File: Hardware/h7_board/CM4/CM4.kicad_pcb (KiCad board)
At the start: 4 copper layers, 68.2 x 41.6 mm, 85 parts, among them IC1 OPA659IDBVR, IC2 OPA659IDBVR, IC3 LMH6643MAX_NOPB, IC4 TPS65133DPDR, IC5 TPS62111RSAT, J1 Conn_Coaxial, J2 USB_C_Receptacle_USB2.0, J3 SWDIO, J4 Micro_SD_Card, J5 PREAMP, J6 BIASED OUTPUT, J7 USART, Q1 AO3401A, U1 USBLC6-2SC6, U2 STM32H743VITx, U3 REF3433IDBVR, Y1 16MHz

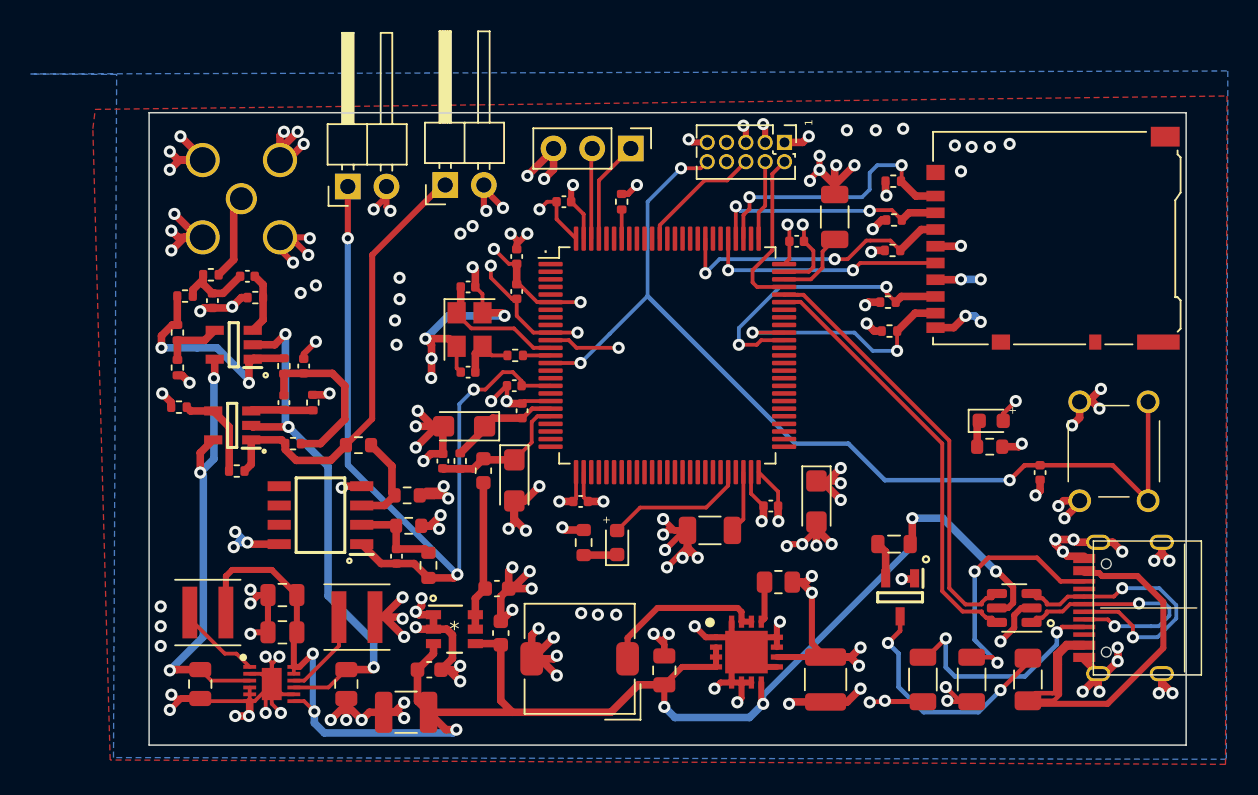
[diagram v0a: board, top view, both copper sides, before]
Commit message: Edited Design to modify to LDO regulator and improve board layout
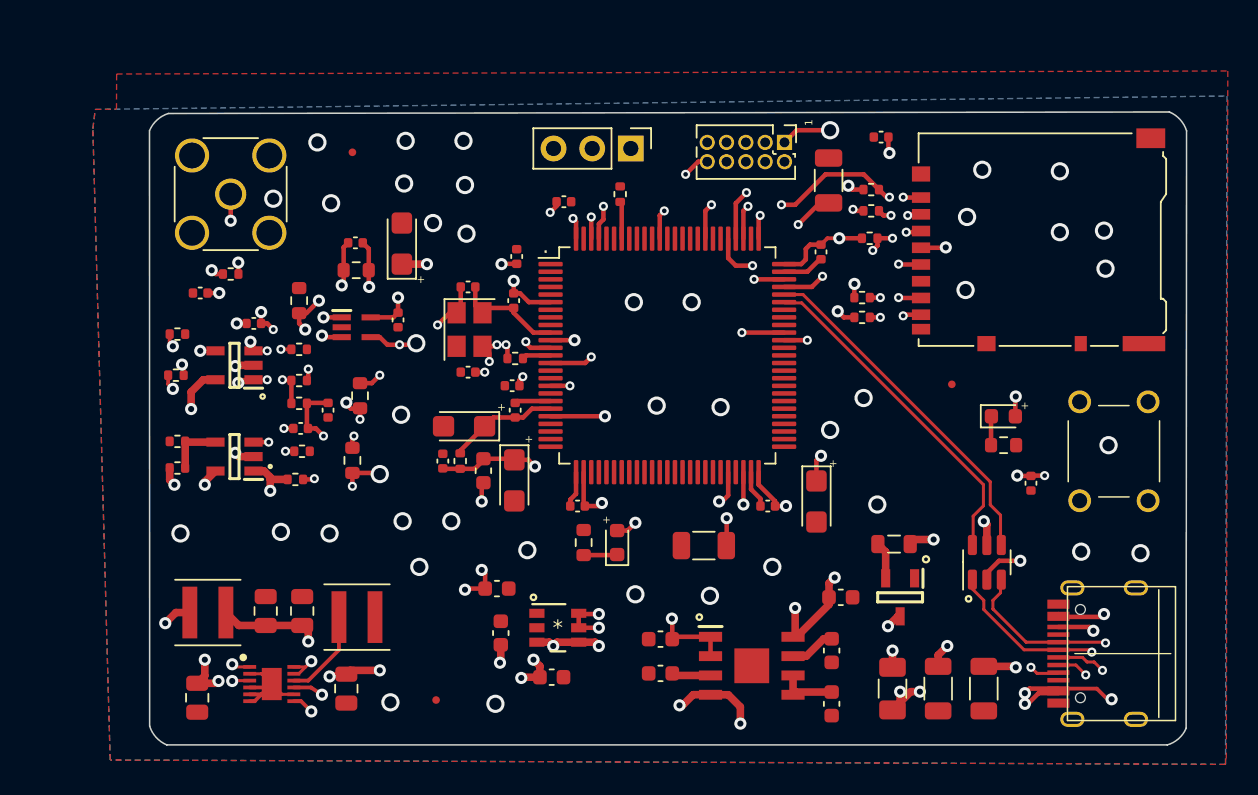
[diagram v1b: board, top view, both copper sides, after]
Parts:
- removed J5: PREAMP, Connector_PinHeader_2.54mm:PinHeader_1x02_P2.54mm_Horizontal
- removed J6: BIASED OUTPUT, Connector_PinHeader_2.54mm:PinHeader_1x02_P2.54mm_Horizontal
- removed L3: 6.8u, Inductor_SMD:L_TDK_SLF7032
- removed R25, R26: 47k, Resistor_SMD:R_0402_1005Metric
- removed U1: USBLC6-2SC6, Package_TO_SOT_SMD:SOT-23-6
- added C30: 100p, Capacitor_SMD:C_0402_1005Metric, F.Cu at (99.5, 87.0)
- added C31: 100p, Capacitor_SMD:C_0402_1005Metric, F.Cu at (109.7, 83.7)
- added C32: 10u, Capacitor_Tantalum_SMD:CP_EIA-3216-18_Kemet-A, F.Cu at (112.8, 83.8)
- added C33: 100n, Capacitor_SMD:C_0402_1005Metric, F.Cu at (112.5, 88.8)
- added C34: 100n, Capacitor_SMD:C_0402_1005Metric, F.Cu at (144.2, 76.8)
- added FID1: Fiducial, Fiducial:Fiducial_0.5mm_Mask1.5mm, F.Cu at (109.5, 77.8)
- added FID2: Fiducial, Fiducial:Fiducial_0.5mm_Mask1.5mm, F.Cu at (115.0, 113.8)
- added FID3: Fiducial, Fiducial:Fiducial_0.5mm_Mask1.5mm, F.Cu at (148.9, 93.0)
- added R19: 47k, Resistor_SMD:R_0402_1005Metric, F.Cu at (143.6, 81.6)
- added U4: USBLC6-2SC6, Package_TO_SOT_SMD:SOT-23-6, F.Cu at (151.2, 104.7)
- C1, C2: value 100p -> 10u; footprint Capacitor_SMD:C_0402_1005Metric -> Capacitor_SMD:C_0603_1608Metric
- C10: value 10u x5R 25V -> 100p; footprint Capacitor_SMD:C_1210_3225Metric -> Capacitor_SMD:C_0402_1005Metric
- C11: value 22u x7R 10V -> 100p; footprint Capacitor_SMD:C_1210_3225Metric -> Capacitor_SMD:C_0402_1005Metric
- C12: value 1u -> 100p; footprint Capacitor_SMD:C_0805_2012Metric -> Capacitor_SMD:C_0402_1005Metric
- C3, C4: value 100p -> 1u; footprint Capacitor_SMD:C_0402_1005Metric -> Capacitor_SMD:C_0603_1608Metric
- C5: value 10p -> 1u; footprint Capacitor_SMD:C_0402_1005Metric -> Capacitor_SMD:C_0603_1608Metric
- IC1: value OPA659IDBVR -> ADP7156ARDZ-3.3-R7; footprint SamacSys_Parts:SOT95P280X145-5N -> SamacSys_Parts:SOIC127P600X175-9N
- IC3: value LMH6643MAX_NOPB -> OPA659IDBVR; footprint SamacSys_Parts:SOIC127P600X175-8N -> SamacSys_Parts:SOT95P280X145-5N
- IC5: value TPS62111RSAT -> OPA377AIDCKR; footprint SamacSys_Parts:QFN65P400X400X100-17N-D -> SamacSys_Parts:SOT65P210X110-5N
- J1: value Conn_Coaxial -> USB_C_Receptacle_USB2.0; footprint Connector_Coaxial:SMA_Wurth_60312002114503_Vertical -> CM4IO:TYPE-C-31-M-12; moved to F.Cu
- J2: value USB_C_Receptacle_USB2.0 -> Conn_Coaxial; footprint CM4IO:TYPE-C-31-M-12 -> Connector_Coaxial:SMA_Wurth_60312002114503_Vertical
- R1: value 44.2k -> 5.1k; footprint Resistor_SMD:R_0402_1005Metric -> Resistor_SMD:R_1206_3216Metric
- R11: value 100k -> 187; footprint Resistor_SMD:R_0603_1608Metric -> Resistor_SMD:R_0402_1005Metric
- R12: value 50k -> 2.49k; footprint Resistor_SMD:R_0603_1608Metric -> Resistor_SMD:R_0402_1005Metric
- R15: value 5.1k -> 49.9k; footprint Resistor_SMD:R_1206_3216Metric -> Resistor_SMD:R_0603_1608Metric
- R16: value 5.1k -> 100k; footprint Resistor_SMD:R_1206_3216Metric -> Resistor_SMD:R_0603_1608Metric
- R17: value 1M -> 47k; footprint Resistor_SMD:R_0805_2012Metric -> Resistor_SMD:R_0402_1005Metric
- R2: value 66.5k -> 5.1k; footprint Resistor_SMD:R_0402_1005Metric -> Resistor_SMD:R_1206_3216Metric
- R3: value 6.34k -> 44.2k
- R4: value 35.7k -> 66.5k
- R5: value 34.8k -> 6.34k
- R6: value 10k -> 35.7k
- R7: value 187 -> 34.8k
- R8: value 2.49k -> 10k
- U3: footprint footprints:REF3433IDBVR -> REF3433:REF3433IDBVR
- moved J2 67.0 mm to (101.5, 80.5), turned to 0 degrees
- moved J1 66.0 mm to (161.0, 110.7)
- moved R2 55.8 mm to (148.0, 113.0), turned to -90 degrees
- moved R16 50.7 mm to (106.0, 87.5), turned to 90 degrees
- moved R1 48.2 mm to (151.0, 113.0), turned to -90 degrees
- moved R15 45.9 mm to (109.8, 85.5), turned to 180 degrees
- moved C2 44.3 mm to (141.6, 107.0), turned to 0 degrees
- moved C11 44.3 mm to (103.0, 89.0), turned to 0 degrees
- moved C3 39.4 mm to (141.0, 110.5), turned to -90 degrees
- moved C4 38.3 mm to (129.8, 112.0), turned to 180 degrees
- moved IC1 37.6 mm to (135.8, 111.5), turned to 0 degrees
- moved IC5 33.4 mm to (109.8, 89.2)
- moved C5 30.2 mm to (141.0, 114.0)
- moved C1 29.2 mm to (129.8, 109.8), turned to 180 degrees
- moved C12 27.9 mm to (107.9, 94.7), turned to -90 degrees
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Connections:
- C1 pad 1: Net-(C1-Pad1) -> /+3.3V
- C1 pad 2: Net-(C1-Pad2) -> GND
- C10 pad 1: /Power/+5V -> Net-(C10-Pad1)
- C10 pad 2: GND -> Net-(C10-Pad2)
- C11 pad 1: /+3.3V -> Net-(C11-Pad1)
- C11 pad 2: GND -> Net-(C11-Pad2)
- C12 pad 1: /Power/+5V -> Net-(C10-Pad2)
- C2 pad 1: Net-(C2-Pad1) -> /Power/+5V
- C2 pad 2: Net-(C2-Pad2) -> GND
- C3 pad 1: Net-(C1-Pad2) -> Net-(C3-Pad1)
- C4 pad 1: Net-(C2-Pad2) -> Net-(C4-Pad1)
- C5 pad 2: /v_DIV_OUT -> GND
- IC1 pad 1: P_AMP_OUT -> /+3.3V
- IC1 pad 2: /VNEG -> /+3.3V
- IC1 pad 3: Net-(C1-Pad1) -> Net-(C4-Pad1)
- IC1 pad 4: Net-(IC1-Pad4) -> /Power/+5V
- IC1 pad 5: /VPOS -> Net-(C5-Pad1)
- IC2 pad 1: Net-(IC2-Pad1) -> P_AMP_OUT
- IC2 pad 3: Net-(C2-Pad1) -> Net-(C10-Pad1)
- IC3 pad 1: /v_DIV_OUT -> Net-(IC3-Pad1)
- IC3 pad 2: Net-(C5-Pad1) -> /VNEG
- IC3 pad 3: Net-(IC3-Pad3) -> Net-(C11-Pad1)
- IC3 pad 4: GND -> Net-(IC3-Pad4)
- IC3 pad 5: no_connect_55 -> /VPOS
- IC5 pad 1: GND -> Net-(IC5-Pad1)
- IC5 pad 2: /Power/+5V -> GND
- IC5 pad 3: /Power/+5V -> Net-(C31-Pad2)
- IC5 pad 4: /Power/+5V -> /v_DIV_OUT
- IC5 pad 5: GND -> /+3.3V
- J3 pad 7: no_connect_60 -> no_connect_58
- J3 pad 8: no_connect_61 -> no_connect_59
- R1 pad 1: P_AMP_OUT -> Net-(J1-PadA5)
- R1 pad 2: Net-(C1-Pad2) -> GND
- R10 pad 1: Net-(IC2-Pad1) -> P_AMP_OUT
- R11 pad 1: GND -> Net-(IC3-Pad4)
- R11 pad 2: Net-(C5-Pad1) -> GND
- R12 pad 1: /v_DIV_OUT -> Net-(IC3-Pad1)
- R12 pad 2: Net-(C5-Pad1) -> Net-(IC3-Pad4)
- R13 pad 1: Net-(IC3-Pad3) -> Net-(IC5-Pad1)
- R14 pad 2: Net-(IC3-Pad3) -> Net-(IC5-Pad1)
- R15 pad 1: Net-(J2-PadA5) -> /v_DIV_OUT
- R15 pad 2: GND -> Net-(C31-Pad2)
- R16 pad 1: Net-(J2-PadB5) -> Net-(C31-Pad2)
- R17 pad 1: /Power/PG -> /H7MCU/SDMMC_D2
- R2 pad 1: Net-(IC2-Pad1) -> Net-(J1-PadB5)
- R2 pad 2: Net-(C2-Pad2) -> GND
- R22 pad 1: /H7MCU/SDMMC_D2 -> /H7MCU/SDMMC_CMD
- R23 pad 1: /H7MCU/SDMMC_D3 -> /H7MCU/SDMMC_D0
- R24 pad 1: /H7MCU/SDMMC_CMD -> /H7MCU/SDMMC_D1
- R3 pad 1: GND -> P_AMP_OUT
- R3 pad 2: Net-(C1-Pad1) -> Net-(C10-Pad2)
- R4 pad 1: Net-(C2-Pad2) -> Net-(IC3-Pad1)
- R4 pad 2: Net-(J1-Pad1) -> Net-(C11-Pad2)
- R5 pad 1: Net-(C1-Pad2) -> GND
- R5 pad 2: Net-(IC2-Pad1) -> Net-(C10-Pad1)
- R6 pad 1: GND -> Net-(C11-Pad2)
- R6 pad 2: Net-(C2-Pad1) -> Net-(J2-Pad1)
- R7 pad 1: Net-(IC1-Pad4) -> Net-(C10-Pad2)
- R7 pad 2: GND -> Net-(IC3-Pad1)
- R8 pad 1: P_AMP_OUT -> GND
- R8 pad 2: Net-(IC1-Pad4) -> Net-(C11-Pad1)
- U2 pad 1: no_connect_62 -> no_connect_60
- U2 pad 15: no_connect_63 -> no_connect_61
- U2 pad 16: no_connect_64 -> no_connect_62
- U2 pad 18: no_connect_65 -> no_connect_63
- U2 pad 2: no_connect_66 -> no_connect_64
- U2 pad 22: no_connect_67 -> no_connect_65
- U2 pad 23: no_connect_68 -> no_connect_66
- U2 pad 24: no_connect_69 -> no_connect_67
- U2 pad 25: no_connect_70 -> no_connect_68
- U2 pad 28: no_connect_71 -> no_connect_69
- U2 pad 29: no_connect_72 -> no_connect_70
- U2 pad 3: no_connect_73 -> no_connect_71
- U2 pad 30: no_connect_74 -> no_connect_72
- U2 pad 31: no_connect_75 -> no_connect_73
- U2 pad 32: no_connect_76 -> no_connect_74
- U2 pad 33: no_connect_77 -> no_connect_75
- U2 pad 34: no_connect_78 -> no_connect_76
- U2 pad 35: no_connect_79 -> no_connect_77
- U2 pad 36: no_connect_80 -> no_connect_78
- U2 pad 37: no_connect_81 -> no_connect_79
- U2 pad 38: no_connect_82 -> no_connect_80
- U2 pad 39: no_connect_83 -> no_connect_81
- U2 pad 4: no_connect_84 -> no_connect_82
- U2 pad 40: no_connect_85 -> no_connect_83
- U2 pad 41: no_connect_86 -> no_connect_84
- U2 pad 42: no_connect_87 -> no_connect_85
- U2 pad 43: no_connect_88 -> no_connect_86
- U2 pad 44: no_connect_89 -> no_connect_87
- U2 pad 45: no_connect_90 -> no_connect_88
- U2 pad 47: no_connect_91 -> no_connect_89
- U2 pad 5: no_connect_92 -> no_connect_90
- U2 pad 51: no_connect_93 -> no_connect_91
- U2 pad 52: no_connect_94 -> no_connect_92
- U2 pad 53: no_connect_95 -> no_connect_93
- U2 pad 54: no_connect_96 -> no_connect_94
- U2 pad 55: no_connect_97 -> no_connect_95
- U2 pad 56: no_connect_98 -> no_connect_96
- U2 pad 57: no_connect_99 -> no_connect_97
- U2 pad 58: no_connect_100 -> no_connect_98
- U2 pad 59: no_connect_101 -> no_connect_99
- U2 pad 60: no_connect_102 -> no_connect_100
- U2 pad 61: no_connect_103 -> no_connect_101
- U2 pad 62: no_connect_104 -> no_connect_102
- U2 pad 63: no_connect_105 -> no_connect_103
- U2 pad 64: no_connect_106 -> no_connect_104
- U2 pad 67: no_connect_107 -> no_connect_105
- U2 pad 68: no_connect_108 -> no_connect_106
- U2 pad 69: no_connect_109 -> no_connect_107
- U2 pad 7: no_connect_110 -> no_connect_108
- U2 pad 77: no_connect_111 -> no_connect_109
- U2 pad 8: no_connect_112 -> no_connect_110
- U2 pad 81: no_connect_113 -> no_connect_111
- U2 pad 82: no_connect_114 -> no_connect_112
- U2 pad 84: no_connect_115 -> no_connect_113
- U2 pad 85: no_connect_116 -> no_connect_114
- U2 pad 86: no_connect_117 -> no_connect_115
- U2 pad 87: no_connect_118 -> no_connect_116
- U2 pad 88: no_connect_119 -> no_connect_117
- U2 pad 9: no_connect_120 -> no_connect_118
- U2 pad 90: no_connect_121 -> no_connect_119
- U2 pad 91: no_connect_122 -> no_connect_120
- U2 pad 92: no_connect_123 -> no_connect_121
- U2 pad 93: no_connect_124 -> no_connect_122
- U2 pad 95: no_connect_125 -> no_connect_123
- U2 pad 96: no_connect_126 -> no_connect_124
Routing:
- net GND: track 295.8 -> 26.6 mm, vias 156 -> 40
- net /+3.3V: track 75.2 -> 47.1 mm, vias 31 -> 21
- net /v_DIV_OUT: track 54.5 -> 27.1 mm, vias 3 -> 5
- net /Power/+5V: track 105.4 -> 86.6 mm, vias 7 -> 14
- net Net-(J2-PadB5): track 16.7 -> 0.00 mm, vias 2 -> 0
- net Net-(J2-PadA5): track 15.1 -> 0.00 mm, vias 2 -> 0
- net Net-(IC2-Pad1): track 14.6 -> 0.00 mm, vias 2 -> 0
- net Net-(J1-PadB5): track 0.00 -> 14.0 mm, vias 0 -> 2
- net Net-(C11-Pad2): track 0.00 -> 12.7 mm, vias 0 -> 5
- net /3.3VREF: track 9.94 -> 22.2 mm, vias 0 -> 5
- net Net-(F1-Pad2): track 16.1 -> 3.89 mm
- net Net-(IC5-Pad1): track 0.00 -> 11.8 mm, vias 0 -> 4
- net Net-(C1-Pad2): track 11.5 -> 0.00 mm
- net Net-(IC3-Pad1): track 0.00 -> 11.4 mm, vias 0 -> 4
- net /Power/SW: track 11.1 -> 0.00 mm
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- added copper zone on In1.Cu, net /+3.3V
- removed copper zone on In1.Cu, net GND
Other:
- outline, holes or cut-outs redrawn
- board text removed: "BIASED SIGNAL"

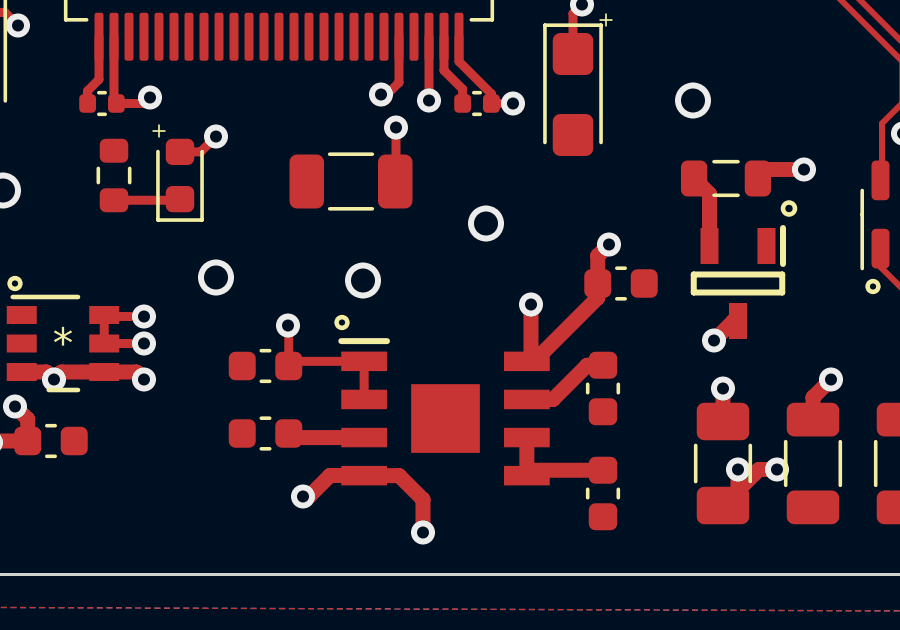
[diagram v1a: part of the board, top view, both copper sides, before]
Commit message: Added Low noise analysis and design files
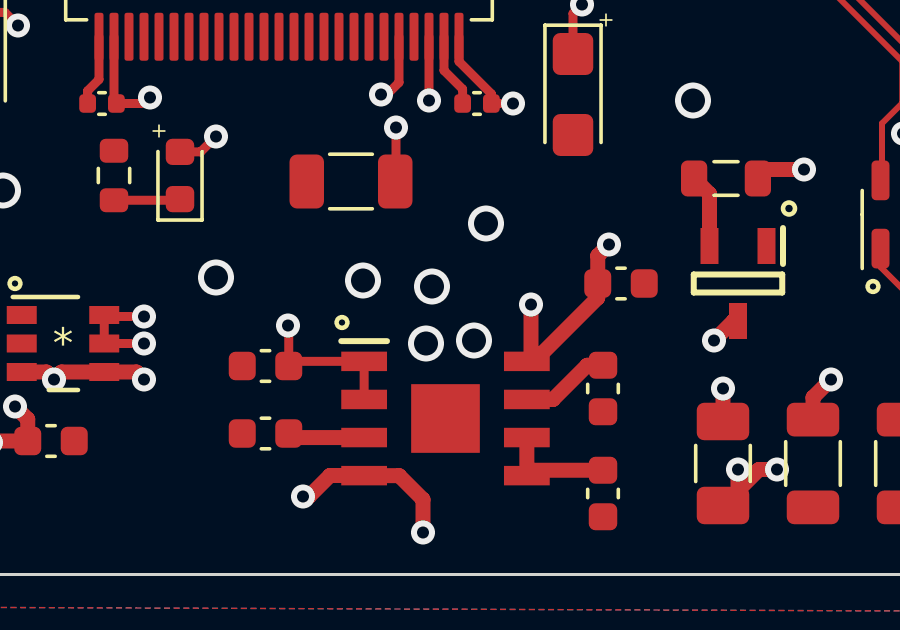
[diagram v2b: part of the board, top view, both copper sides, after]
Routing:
- net GND: vias 40 -> 43
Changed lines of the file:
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@@
     (descr "Tantalum Capacitor SMD Kemet-A (3216-18 Metric), IPC_7351 nominal, (Body size from: http://www.kemet.com/Lists/ProductCatalog/Attachments/253/KEM_TC101_STD.pdf), generated with kicad-footprint-generator")
     (tags "capacitor tantalum")
+    (property "LCSC Part #" "C7171")
     (property "Sheet file" "preamp.kicad_sch")
     (property "Sheet name" "Preamp")
@@
     (at 161 110.7 90)
     (descr "Korean Hroparts Elec, Power only USB connector supporting up to 3A")
+    (property "LCSC Part #" " C165948")
     (property "Sheet file" "power.kicad_sch")
     (property "Sheet name" "Power")
@@
     (descr "Capacitor SMD 0603 (1608 Metric), square (rectangular) end terminal, IPC_7351 nominal, (Body size source: IPC-SM-782 page 76, https://www.pcb-3d.com/wordpress/wp-content/uploads/ipc-sm-782a_amendment_1_and_2.pdf), generated with kicad-footprint-generator")
     (tags "capacitor")
-    (property "LCSC Part #" "C15849")
+    (property "LCSC Part #" "C19702")
     (property "Sheet file" "power.kicad_sch")
     (property "Sheet name" "Power")
@@
     (descr "Capacitor SMD 0603 (1608 Metric), square (rectangular) end terminal, IPC_7351 nominal, (Body size source: IPC-SM-782 page 76, https://www.pcb-3d.com/wordpress/wp-content/uploads/ipc-sm-782a_amendment_1_and_2.pdf), generated with kicad-footprint-generator")
     (tags "capacitor")
-    (property "LCSC Part #" "C15849")
+    (property "LCSC Part #" "C19702")
     (property "Sheet file" "power.kicad_sch")
     (property "Sheet name" "Power")
@@
   (via (at 108.1 81.1) (size 1.2) (drill 0.8) (layers "F.Cu" "B.Cu") (free) (net 1))
   (via (at 121 103.9) (size 1.2) (drill 0.8) (layers "F.Cu" "B.Cu") (free) (net 1))
+  (via (at 135.1 109) (size 1.2) (drill 0.8) (layers "F.Cu" "B.Cu") (free) (net 1))
+  (via (at 135.3 107.1) (size 1.2) (drill 0.8) (layers "F.Cu" "B.Cu") (free) (net 1))
   (via (at 159.2 97) (size 1.2) (drill 0.8) (layers "F.Cu" "B.Cu") (free) (net 1))
   (via (at 114.8 82.4) (size 1.2) (drill 0.8) (layers "F.Cu" "B.Cu") (free) (net 1))
@@
   (via (at 104.3 80.8) (size 1.2) (drill 0.8) (layers "F.Cu" "B.Cu") (free) (net 1))
   (via (at 143.1 93.9) (size 1.2) (drill 0.8) (layers "F.Cu" "B.Cu") (free) (net 1))
+  (via (at 136.7 108.9) (size 1.2) (drill 0.8) (layers "F.Cu" "B.Cu") (free) (net 1))
   (via (at 118.9 114) (size 1.2) (drill 0.8) (layers "F.Cu" "B.Cu") (free) (net 1))
   (via (at 158.9 82.9) (size 1.2) (drill 0.8) (layers "F.Cu" "B.Cu") (free) (net 1))
@@
   (segment (start 136.6 81.6) (end 136.6 78.4) (width 0.3) (layer "In1.Cu") (net 70))
   (segment (start 136.3 81.9) (end 136.6 81.6) (width 0.3) (layer "In1.Cu") (net 70))
-  (segment (start 136.6 78.4) (end 136.63 78.37) (width 0.3) (layer "In1.Cu") (net 70))
   (segment (start 139.7 86.6) (end 140.4 85.9) (width 0.3) (layer "F.Cu") (net 71))
   (segment (start 137.875 86.6) (end 139.7 86.6) (width 0.3) (layer "F.Cu") (net 71))
